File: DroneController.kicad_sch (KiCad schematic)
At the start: 29 parts, among them P1 USB_C_Plug, U2 L80-R, U3 BMP280, U4 MPU-6500, Y1 8Mhz

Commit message: testing webhooks
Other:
- note added: "test"
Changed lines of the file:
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@@
+		)
+	)
+	(text "test"
+		(exclude_from_sim no)
+		(at 195.834 48.26 0)
+		(effects
+			(font
+				(size 0.01 0.01)
+			)
 		)
 	)

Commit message: testing webhooks #2
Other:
- note removed: "test"
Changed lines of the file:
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@@
-		)
-	)
-	(text "test"
-		(exclude_from_sim no)
-		(at 195.834 48.26 0)
-		(effects
-			(font
-				(size 0.01 0.01)
-			)
 		)
 	)

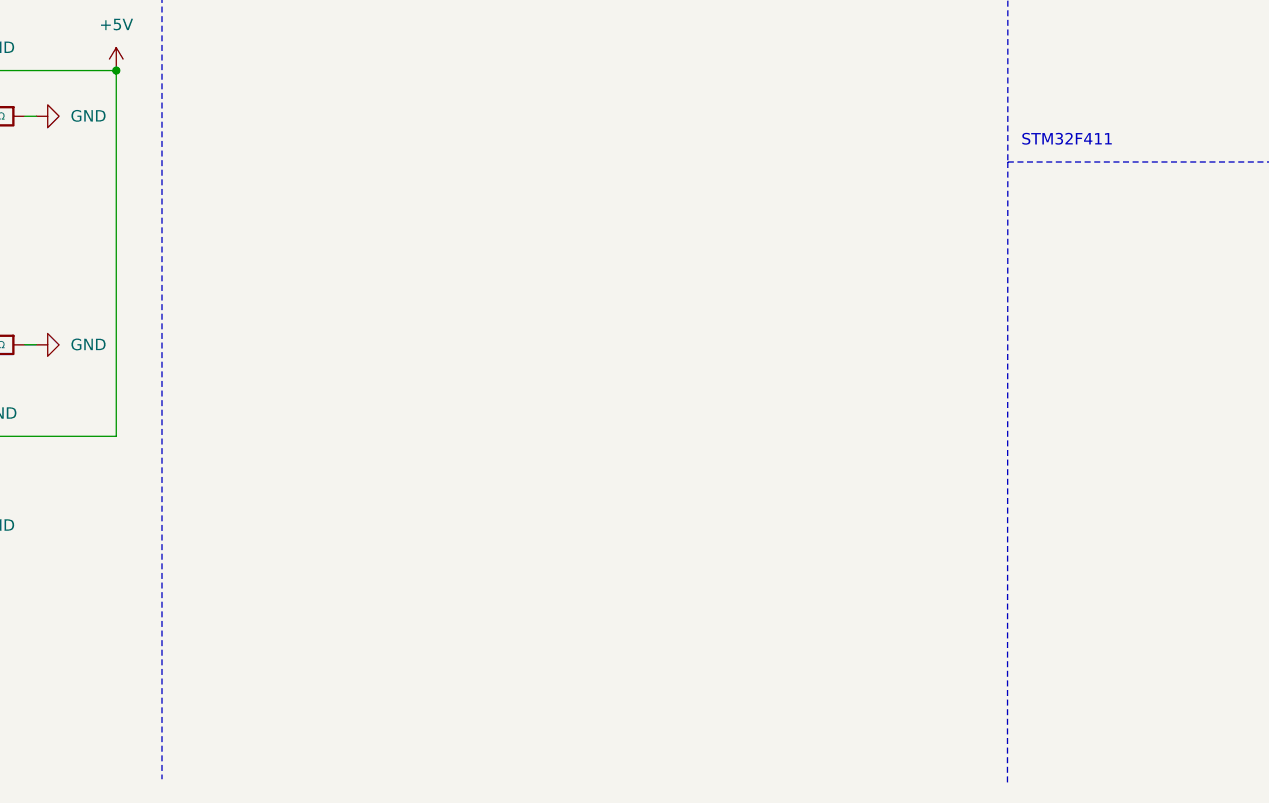
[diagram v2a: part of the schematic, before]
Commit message: Added Buck Converter
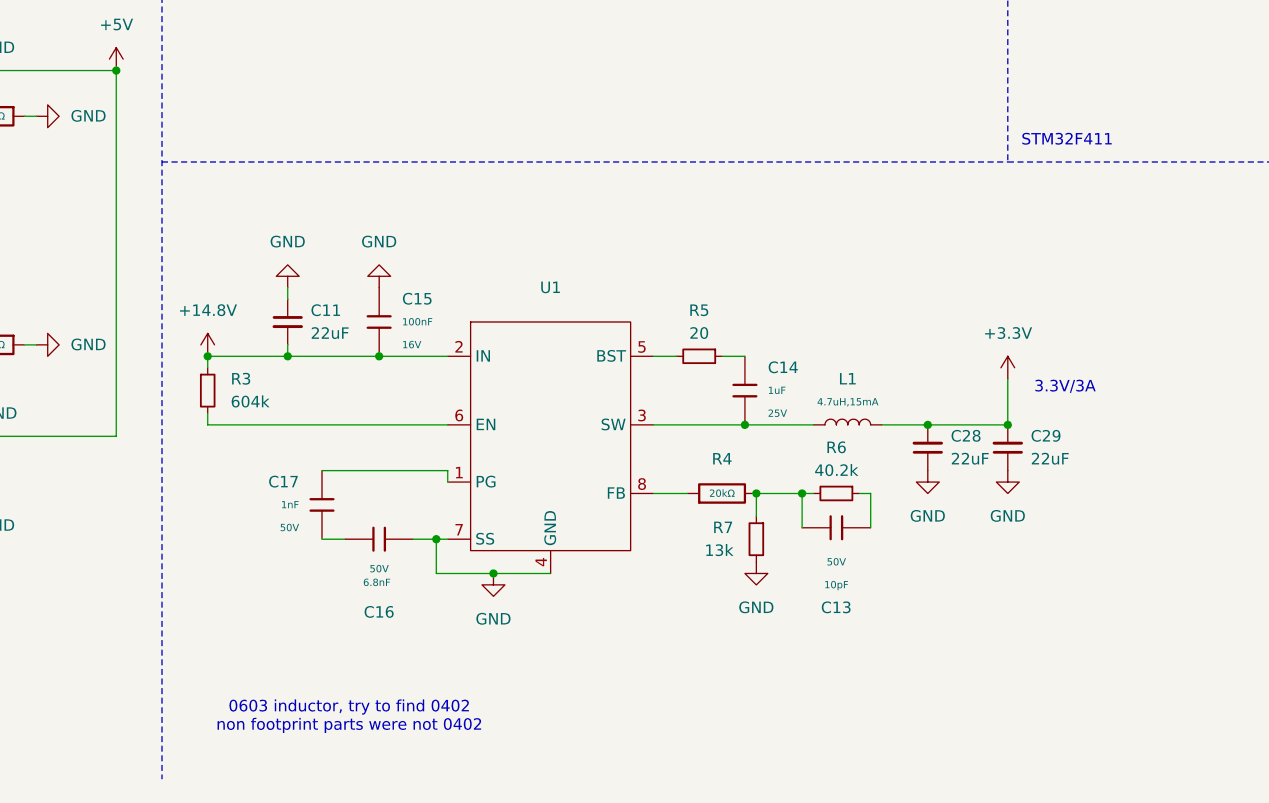
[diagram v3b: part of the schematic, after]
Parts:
- added C11, C28, C29: 22uF, symbol Device:C_Small
- added C13: 10pF, PCM_JLCPCB:C_0402, symbol PCM_JLCPCB-Capacitors:0402,10pF
- added C14: 1uF, PCM_JLCPCB:C_0402, symbol PCM_JLCPCB-Capacitors:0402,1uF
- added C15: 100nF, PCM_JLCPCB:C_0402, symbol PCM_JLCPCB-Capacitors:0402,100nF
- added C16: 6.8nF, PCM_JLCPCB:C_0402, symbol PCM_JLCPCB-Capacitors:0402,6.8nF
- added C17: 1nF, PCM_JLCPCB:C_0402, symbol PCM_JLCPCB-Capacitors:0402,1nF
- added L1: 4.7uH,15mA, PCM_JLCPCB:L_0603, symbol PCM_JLCPCB-Inductors:4.7uH,15mA
- added R3: 604k, symbol Device:R_Small
- added R4: 20kΩ, PCM_JLCPCB:R_0402, symbol PCM_JLCPCB-Resistors:0402,20kΩ
- added R5: 20, symbol Device:R_Small
- added R6: 40.2k, symbol Device:R_Small
- added R7: 13k, symbol Device:R_Small
- added U1: ~, symbol MP2393buckConverter:MP2393buckConverter
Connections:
- net +3.3V: now also C28.2, C29.2, L1.2
- net GND: now also C11.1, C15.1, C16.2, C28.1, C29.1, R7.2, U1.4 (GND), U1.7 (SS)
- new net: C14.2, L1.1, U1.3 (SW)
- new net: R3.2, U1.6 (EN)
- new net: C13.1, R4.2, R6.2, R7.1
- new net: C13.2, R6.1
- new net: C16.1, C17.2
- new net: C17.1, U1.1 (PG)
- new net: R5.2, U1.5 (BST)
- new net: R4.1, U1.8 (FB)
- new net: C14.1, R5.1
- new net +14.8V: C11.2, C15.2, R3.1, U1.2 (IN)
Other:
- note added: "0603 inductor, try to find 0402 non footprint parts were not 0402"
- note added: "3.3V/3A"

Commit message: Finalized sensor board schematic
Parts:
- removed C15: 100nF, PCM_JLCPCB:C_0402, symbol PCM_JLCPCB-Capacitors:0402,100nF
- removed R7: 13k, symbol Device:R_Small
- added C30: 100nF, PCM_JLCPCB:C_0402, symbol PCM_JLCPCB-Capacitors:0402,100nF,(2)
- added R8: 13kΩ, PCM_JLCPCB:R_0402, symbol PCM_JLCPCB-Resistors:0603,13kΩ
- C11: footprint (none) -> Capacitor_SMD:C_0603_1608Metric; LCSC (none) -> C14663
- C28: footprint (none) -> Capacitor_SMD:C_0603_1608Metric
- R3: footprint (none) -> Resistor_SMD:R_0402_1005Metric; LCSC (none) -> C27013
- R5: footprint (none) -> PCM_JLCPCB:R_0603; LCSC (none) -> C22950
- R6: footprint (none) -> PCM_JLCPCB:R_0402; LCSC (none) -> C25893
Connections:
- net +14.8V: now also C30.2
- net GND: now also C30.1, R8.2
- net at C13.1, R4.2, R6.2: now also R8.1
- no-connect marks 27 -> 31
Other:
- note added: "22uF, 20ohm and inductor are 0603"
- note added: "Drone Sensor Board"
- note added: "MP2393GTL-Z"
- note removed: "0603 inductor, try to find 0402 non footprint parts were not 0402"
- moved on the sheet: C11, C13, C14, C16, C17, C18, C22, C23, C24, C25, C28, C29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
